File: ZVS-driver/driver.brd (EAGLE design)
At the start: 17 parts, among them Q1 10N60, Q2 10N60

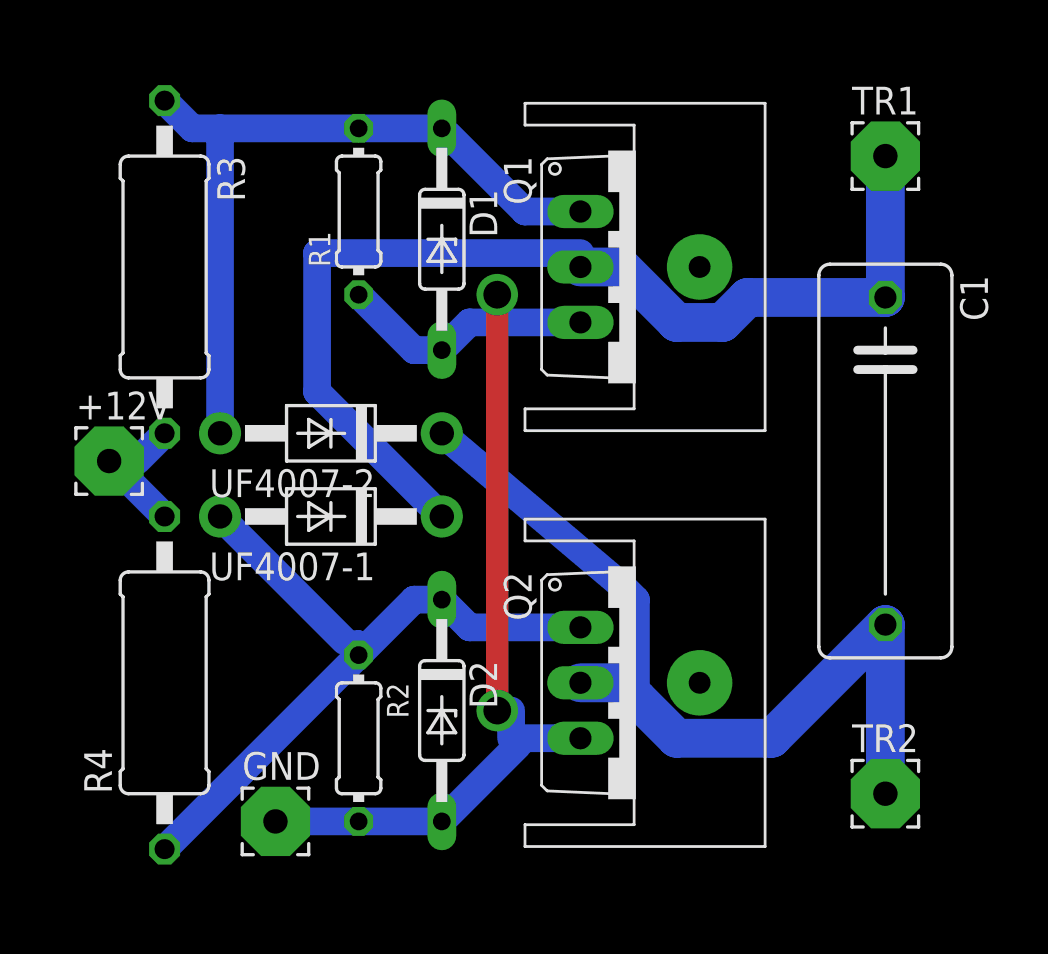
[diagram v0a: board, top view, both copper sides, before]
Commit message: ZVS-driver updated
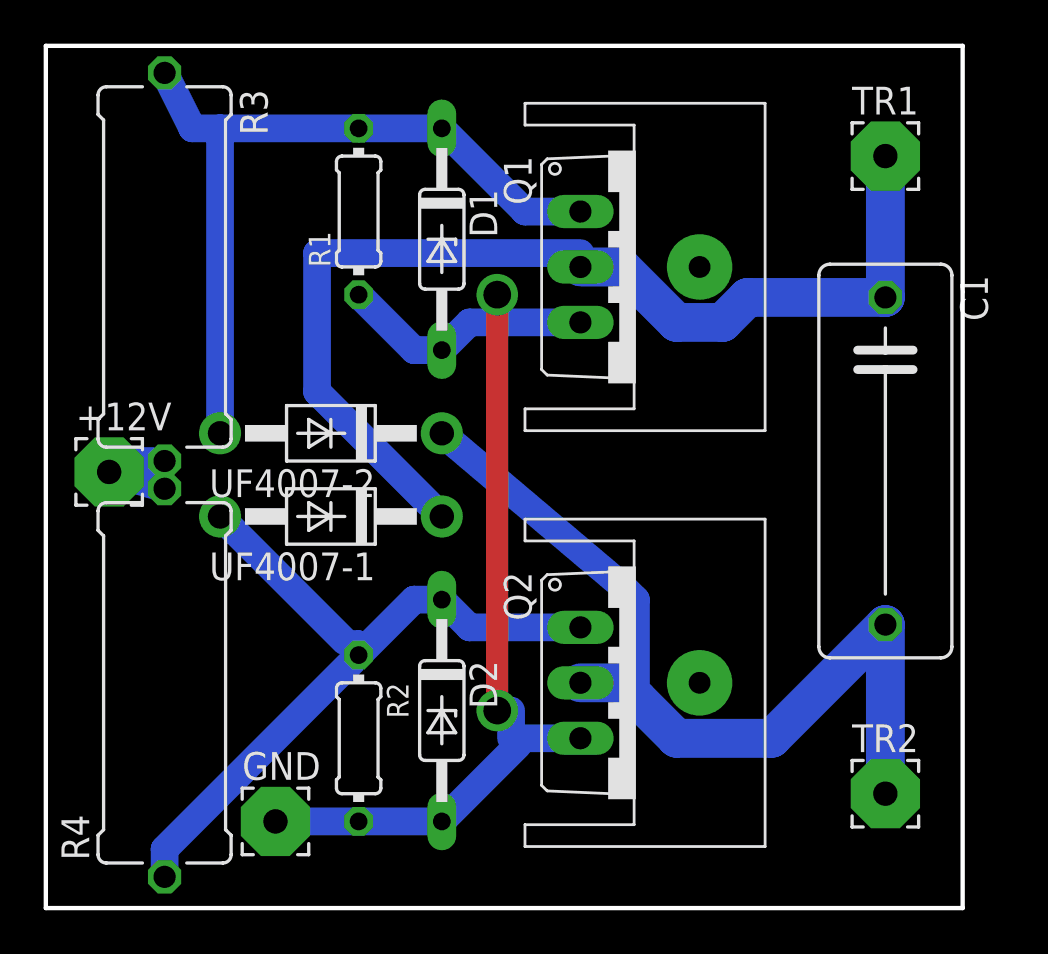
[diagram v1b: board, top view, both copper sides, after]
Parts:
- R3, R4: device resistor:0411/15 -> resistor:0617/17
- moved +12V 0.50 mm to (88.9, 30.0)
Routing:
- net N$3: track 6.66 -> 5.29 mm
- net N$4: track 33.7 -> 34.9 mm
- net N$2: track 35.1 -> 36.2 mm
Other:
- board outline added: 42 x 39.5 mm
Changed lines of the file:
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@@
 <setting verticaltext="up"/>
 </settings>
-<grid distance="50" unitdist="mil" unit="mil" style="lines" multiple="1" display="no" altdistance="5" altunitdist="mil" altunit="mil"/>
+<grid distance="0.5" unitdist="mm" unit="mm" style="lines" multiple="1" display="no" altdistance="5" altunitdist="mil" altunit="mm"/>
 <layers>
 <layer number="1" name="Top" color="4" fill="1" visible="yes" active="yes"/>
@@
 <board>
 <plain>
+<wire x1="86" y1="49.5" x2="128" y2="49.5" width="0.2" layer="20"/>
+<wire x1="128" y1="49.5" x2="128" y2="10" width="0.2" layer="20"/>
+<wire x1="128" y1="10" x2="86" y2="10" width="0.2" layer="20"/>
+<wire x1="86" y1="10" x2="86" y2="49.5" width="0.2" layer="20"/>
 </plain>
 <attributes>
@@
 <element name="R1" library="resistor" library_urn="urn:adsk.eagle:library:348" package="0204/7" package3d_urn="urn:adsk.eagle:package:25945/1" value="10k" x="100.33" y="41.91" rot="R90"/>
 <element name="R2" library="resistor" library_urn="urn:adsk.eagle:library:348" package="0204/7" package3d_urn="urn:adsk.eagle:package:25945/1" value="10k" x="100.33" y="17.78" rot="R270"/>
-<element name="R3" library="resistor" library_urn="urn:adsk.eagle:library:348" package="0411/15" package3d_urn="urn:adsk.eagle:package:26093/1" value="470" x="91.44" y="39.37" rot="R270"/>
-<element name="R4" library="resistor" library_urn="urn:adsk.eagle:library:348" package="0411/15" package3d_urn="urn:adsk.eagle:package:26093/1" value="470" x="91.44" y="20.32" rot="R90"/>
+<element name="R3" library="resistor" library_urn="urn:adsk.eagle:library:348" package="0617/17" package3d_urn="urn:adsk.eagle:package:26096/1" value="470" x="91.44" y="39.37" rot="R270"/>
+<element name="R4" library="resistor" library_urn="urn:adsk.eagle:library:348" package="0617/17" package3d_urn="urn:adsk.eagle:package:26096/1" value="470" x="91.44" y="20.32" rot="R90"/>
 <element name="D1" library="diode" library_urn="urn:adsk.eagle:library:210" package="DO35Z10" package3d_urn="urn:adsk.eagle:package:43342/1" value="15v" x="104.14" y="40.64" rot="R270"/>
 <element name="D2" library="diode" library_urn="urn:adsk.eagle:library:210" package="DO35Z10" package3d_urn="urn:adsk.eagle:package:43342/1" value="15v" x="104.14" y="19.05" rot="R270"/>
@@
 <element name="TR2" library="wirepad" library_urn="urn:adsk.eagle:library:412" package="3,17/1,1" package3d_urn="urn:adsk.eagle:package:30832/1" value="" x="124.46" y="15.24"/>
 <element name="GND" library="wirepad" library_urn="urn:adsk.eagle:library:412" package="3,17/1,1" package3d_urn="urn:adsk.eagle:package:30832/1" value="" x="96.52" y="13.97"/>
-<element name="+12V" library="wirepad" library_urn="urn:adsk.eagle:library:412" package="3,17/1,1" package3d_urn="urn:adsk.eagle:package:30832/1" value="" x="88.9" y="30.48"/>
+<element name="+12V" library="wirepad" library_urn="urn:adsk.eagle:library:412" package="3,17/1,1" package3d_urn="urn:adsk.eagle:package:30832/1" value="" x="88.9" y="29.98"/>
 <element name="U$1" library="mgvc" package="RAD15X11" value="RADIATOR" x="107.95" y="39.37"/>
 <element name="U$2" library="mgvc" package="RAD15X11" value="RADIATOR" x="107.95" y="20.32"/>
@@
 <wire x1="107.95" y1="41.91" x2="104.14" y2="45.72" width="1.27" layer="16"/>
 <wire x1="104.14" y1="45.72" x2="100.33" y2="45.72" width="1.27" layer="16"/>
-<wire x1="92.71" y1="45.72" x2="91.44" y2="46.99" width="1.27" layer="16"/>
+<wire x1="92.71" y1="45.72" x2="91.44" y2="48.26" width="1.27" layer="16"/>
 <wire x1="100.33" y1="45.72" x2="93.98" y2="45.72" width="1.27" layer="16"/>
 <wire x1="93.98" y1="45.72" x2="92.71" y2="45.72" width="1.27" layer="16"/>
@@
 <wire x1="105.41" y1="22.86" x2="104.14" y2="24.13" width="1.27" layer="16"/>
 <wire x1="104.14" y1="24.13" x2="102.87" y2="24.13" width="1.27" layer="16"/>
-<wire x1="102.87" y1="24.13" x2="100.33" y2="21.59" width="1.27" layer="16"/>
-<wire x1="100.33" y1="21.59" x2="91.44" y2="12.7" width="1.27" layer="16"/>
+<wire x1="100.33" y1="21.59" x2="102.87" y2="24.13" width="1.27" layer="16"/>
 <wire x1="99.695" y1="22.225" x2="93.98" y2="27.94" width="1.27" layer="16"/>
 <wire x1="100.33" y1="22.225" x2="99.695" y2="22.225" width="1" layer="16"/>
 <wire x1="100.33" y1="22.225" x2="100.33" y2="21.59" width="1" layer="16"/>
+<wire x1="91.44" y1="11.43" x2="91.44" y2="12.7" width="1.27" layer="16"/>
+<wire x1="91.44" y1="12.7" x2="100.33" y2="21.59" width="1.27" layer="16"/>
 </signal>
 <signal name="N$6">
@@
 <contactref element="+12V" pad="1"/>
 <contactref element="R4" pad="2"/>
-<wire x1="88.9" y1="30.48" x2="91.44" y2="27.94" width="1.27" layer="16"/>
-<wire x1="90.17" y1="30.48" x2="91.44" y2="31.75" width="1.27" layer="16"/>
-<wire x1="90.17" y1="30.48" x2="88.9" y2="30.48" width="1" layer="16"/>
+<wire x1="88.9" y1="29.98" x2="91.44" y2="29.21" width="1.27" layer="16"/>
+<wire x1="90.17" y1="30.48" x2="91.44" y2="30.48" width="1.27" layer="16"/>
+<wire x1="90.17" y1="30.48" x2="88.9" y2="29.98" width="1" layer="16"/>
 </signal>
 </signals>
